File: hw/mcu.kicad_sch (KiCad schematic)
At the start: 28 parts, among them J2 Conn_01x01, J3 Conn_01x06, Q2 BC846SF, U1 esp-12f

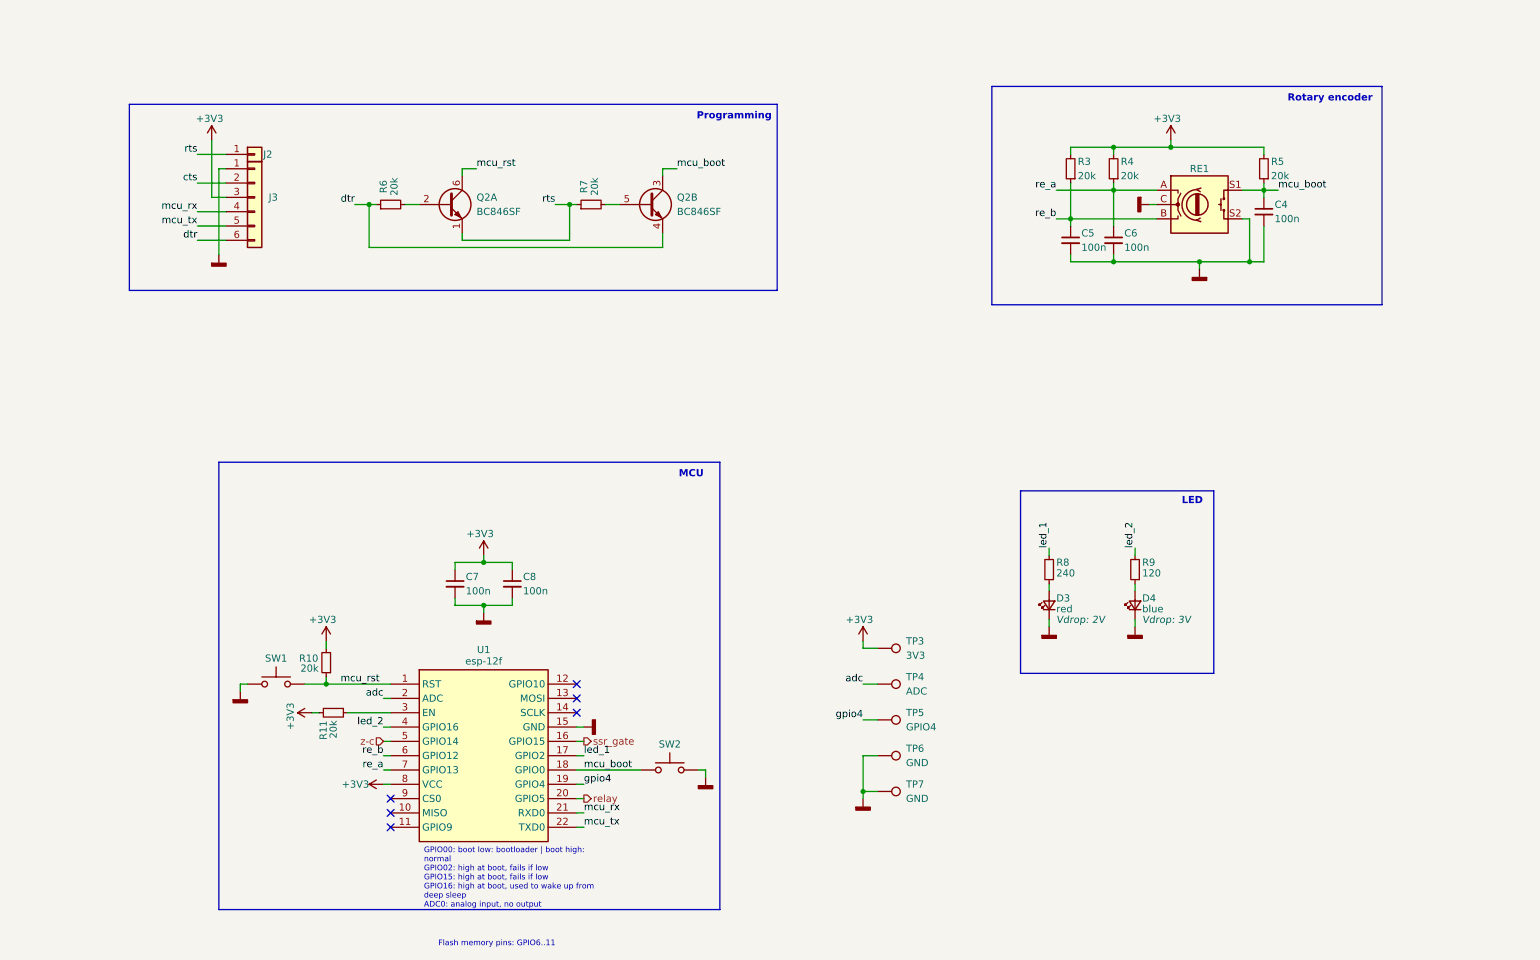
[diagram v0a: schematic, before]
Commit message: V2.0 (#2)
* **Hardware & Mechanical Design**
  * Updated design files and exports.
  * Split chassis and top plate into variants.
  * Changed enclosure folder structure.
  * Hid alignment/dimension layers; removed duplicate models.
  * Added mechanical parts and notes to schematics.

* **Firmware**
  * Updated firmware and added new versions.
  * Introduced firmware variants and consolidated them into packages.
  * Added common.yaml.
  * Moved effects out of packages.

* **Project Structure & Tooling**
  * Added BOM exports and fixed script permissions.
  * Updated and cleaned export folders.
  * Added ESPHome auto-generated `.gitignore`.
  * Fixed included libraries.
  * Miscellaneous corrections, reviews, merges, and cleanup commits.

* **Documentation & README**
  * Multiple revisions for clarity, formatting, structure, and consistency.
  * Added safety warnings for mains voltage operation.
  * Updated table of contents, badges, links, images, and repository structure sections.
  * Added roadmap, split release and change logs, reformatted release log.
  * Added links to schematic, PCB, BOMs, and iBOM.
  * Added additional documentation files.

* **Images, Photos & Media**
  * Updated, renamed, resized, and reformatted images.
  * Improved README image layout (width adjustments, centering, reduced size).
  * Added photos and screenshots across README and sub-readmes.
  * Added animations and animation exports; removed obsolete images.
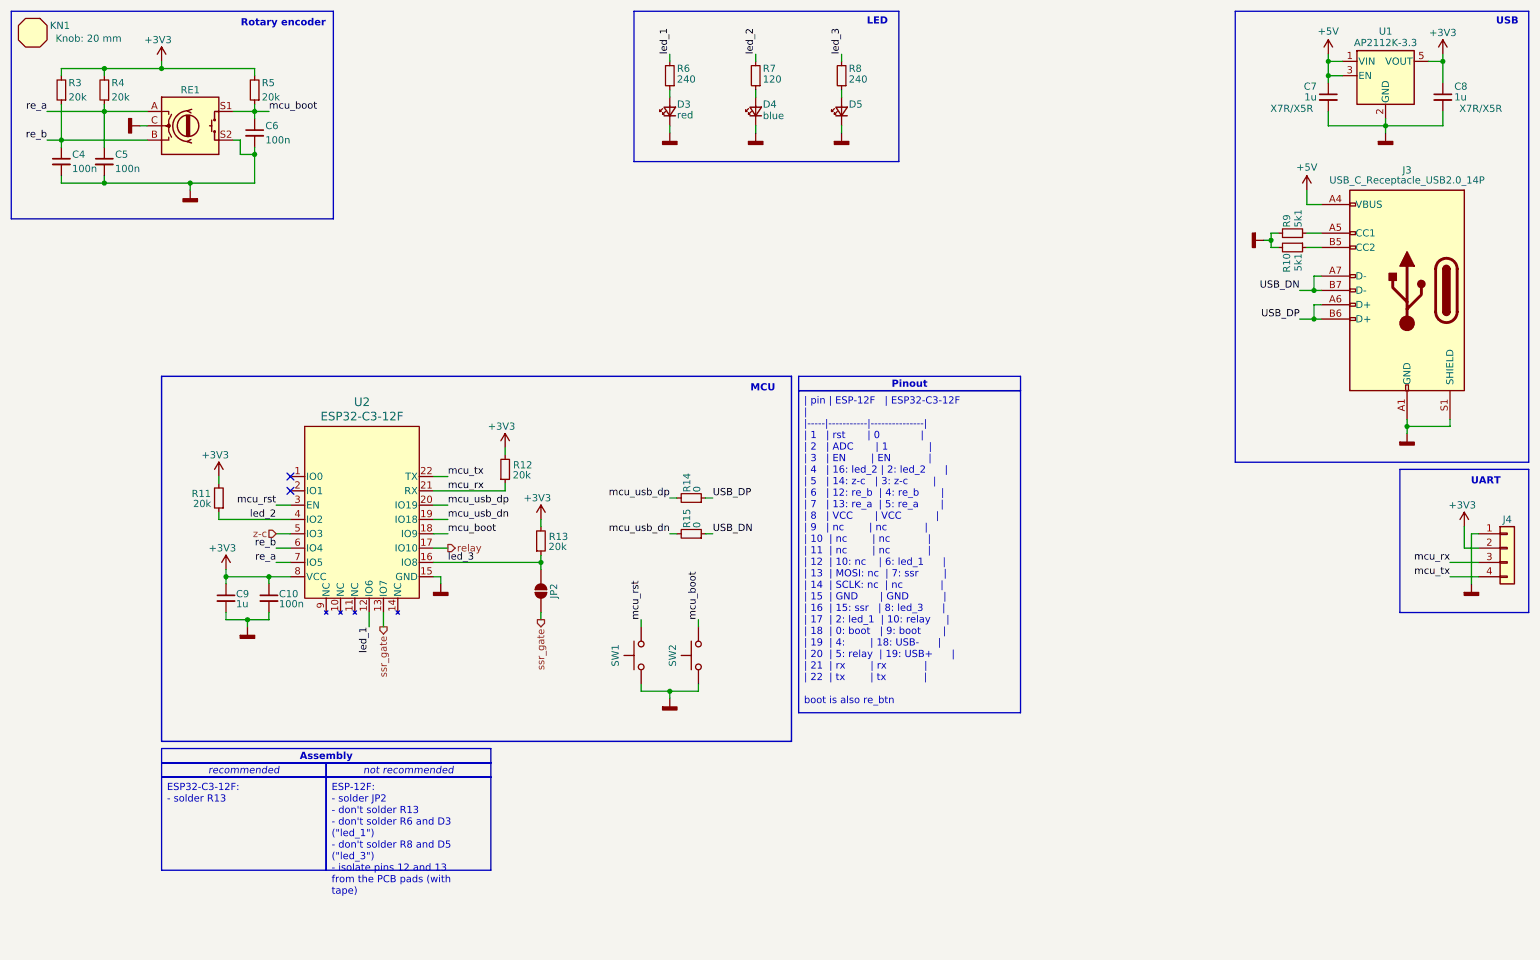
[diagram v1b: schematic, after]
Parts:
- removed J2: Conn_01x01, Connector_Wire:SolderWire-0.1sqmm_1x01_D0.4mm_OD1mm, symbol Connector_Generic:Conn_01x01
- removed Q2: BC846SF, Package_TO_SOT_SMD:SOT-363_SC-70-6_Handsoldering, symbol Device:Q_Dual_NPN_NPN_E1B1C2E2B2C1
- removed R6, R7: 20k, Resistor_SMD:R_0805_2012Metric_Pad1.20x1.40mm_HandSolder, symbol Device:R_Small
- removed TP3: 3V3, TestPoint:TestPoint_Pad_1.0x1.0mm, symbol Connector:TestPoint
- removed TP4: ADC, TestPoint:TestPoint_Pad_1.0x1.0mm, symbol Connector:TestPoint
- removed TP5: GPIO4, TestPoint:TestPoint_Pad_1.0x1.0mm, symbol Connector:TestPoint
- removed TP6, TP7: GND, TestPoint:TestPoint_Pad_1.0x1.0mm, symbol Connector:TestPoint
- removed U1: esp-12f, ESP-12F:esp12f, symbol esp-12f:esp-12f
- added C7, C8: 1u, Capacitor_SMD:C_0805_2012Metric_Pad1.18x1.45mm_HandSolder, symbol Device:C_Small
- added D5: ~, LED_SMD:LED_0805_2012Metric_Pad1.15x1.40mm_HandSolder, symbol Device:LED_Small
- added J3: USB_C_Receptacle_USB2.0_14P, Connector_USB:USB_C_Receptacle_GCT_USB4110, symbol Connector:USB_C_Receptacle_USB2.0_14P
- added JP2: SolderJumper_2_Open, Jumper:SolderJumper-2_P1.3mm_Open_RoundedPad1.0x1.5mm, symbol Jumper:SolderJumper_2_Open
- added KN1: 20 mm, symbol Mechanical:Mechanical_Shape
- added R12, R13: 20k, Resistor_SMD:R_0805_2012Metric_Pad1.20x1.40mm_HandSolder, symbol Device:R_Small
- added R14, R15: 0, Resistor_SMD:R_0805_2012Metric_Pad1.20x1.40mm_HandSolder, symbol Device:R_Small
- added R8: 240, Resistor_SMD:R_0805_2012Metric_Pad1.20x1.40mm_HandSolder, symbol Device:R_Small
- added R9: 5k1, Resistor_SMD:R_0805_2012Metric_Pad1.20x1.40mm_HandSolder, symbol Device:R_Small
- added U1: AP2112K-3.3, Package_TO_SOT_SMD:SOT-23-5, symbol Regulator_Linear:AP2112K-3.3
- added U2: ESP32-C3-12F, ESP32-C3-12F_RFS, symbol ESP32-C3-12F:ESP32-C3-12F
- C9: renamed from C8; value 100n -> 1u
- J4: renamed from J3; footprint Connector_PinHeader_2.54mm:PinHeader_1x06_P2.54mm_Vertical -> Connector_PinHeader_2.54mm:PinHeader_1x04_P2.54mm_Vertical; symbol Connector_Generic:Conn_01x06 -> Connector_Generic:Conn_01x04; now in the parts list
- R10: value 20k -> 5k1
- renumbered C7 to C10, C5 to C4, C6 to C5, C4 to C6, R8 to R6, R9 to R7
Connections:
- net  cts is gone; now on net +3V3: J4.2 (Pin_2)
- net +3V3: now also C8.1, R12.2, R13.2, U1.5 (VOUT), U2.8 (VCC); no longer J4.3 (Pin_3), R10.2
- net GNDD: now also R10.2, SW2.1, C7.2, C8.2, D5.1 (K), J3.A1 (GND), J3.A12 (GND), J3.B1 (GND), J3.B12 (GND), J3.S1 (SHIELD), R9.2, U1.2 (GND), U2.15 (GND); no longer SW2.2
- net led_1: now also U2.12 (IO6)
- net led_2: now also R11.1, U2.4 (IO2)
- net mcu_boot: now also SW2.2, U2.18 (IO9); no longer SW2.1
- net mcu_rst: now also U2.3 (EN); no longer R10.1
- net mcu_rx: now also J4.3 (Pin_3), R12.1, U2.21 (RX); no longer J4.4 (Pin_4)
- net mcu_tx: now also J4.4 (Pin_4), U2.22 (TX); no longer J4.5 (Pin_5)
- net re_a: now also U2.7 (IO5)
- net re_b: now also U2.6 (IO4)
- net relay: now also U2.17 (IO10)
- net ssr_gate: now also JP2.2 (B), U2.13 (IO7)
- net z-c: now also U2.5 (IO3)
- removed net dtr: J4.6 (Pin_6)
- new net: J3.A5 (CC1), R9.1
- new net: J3.B5 (CC2), R10.1
- new net: D5.2 (A), R8.1
- new net +5V: C7.1, J3.A4 (VBUS), J3.A9 (VBUS), J3.B4 (VBUS), J3.B9 (VBUS), U1.1 (VIN), U1.3 (EN)
- new net USB_DN: J3.A7 (D-), J3.B7 (D-), R15.1
- new net USB_DP: J3.A6 (D+), J3.B6 (D+), R14.1
- new net led_3: JP2.1 (A), R13.1, R8.2, U2.16 (IO8)
- new net mcu_usb_dn: R15.2, U2.19 (IO18)
- new net mcu_usb_dp: R14.2, U2.20 (IO19)
- no-connect marks 6 -> 2
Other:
- title: LEDDs -> MCU
- moved on the sheet: C10, C4, C5, C6, C9, D3, D4, R3, R4, R5, R6, R7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
